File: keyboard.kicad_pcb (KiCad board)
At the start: 2 copper layers, 305.7 x 121 mm, 175 parts, among them J1 Conn_02x20_Odd_Even, J2 USB_C_Receptacle_16P

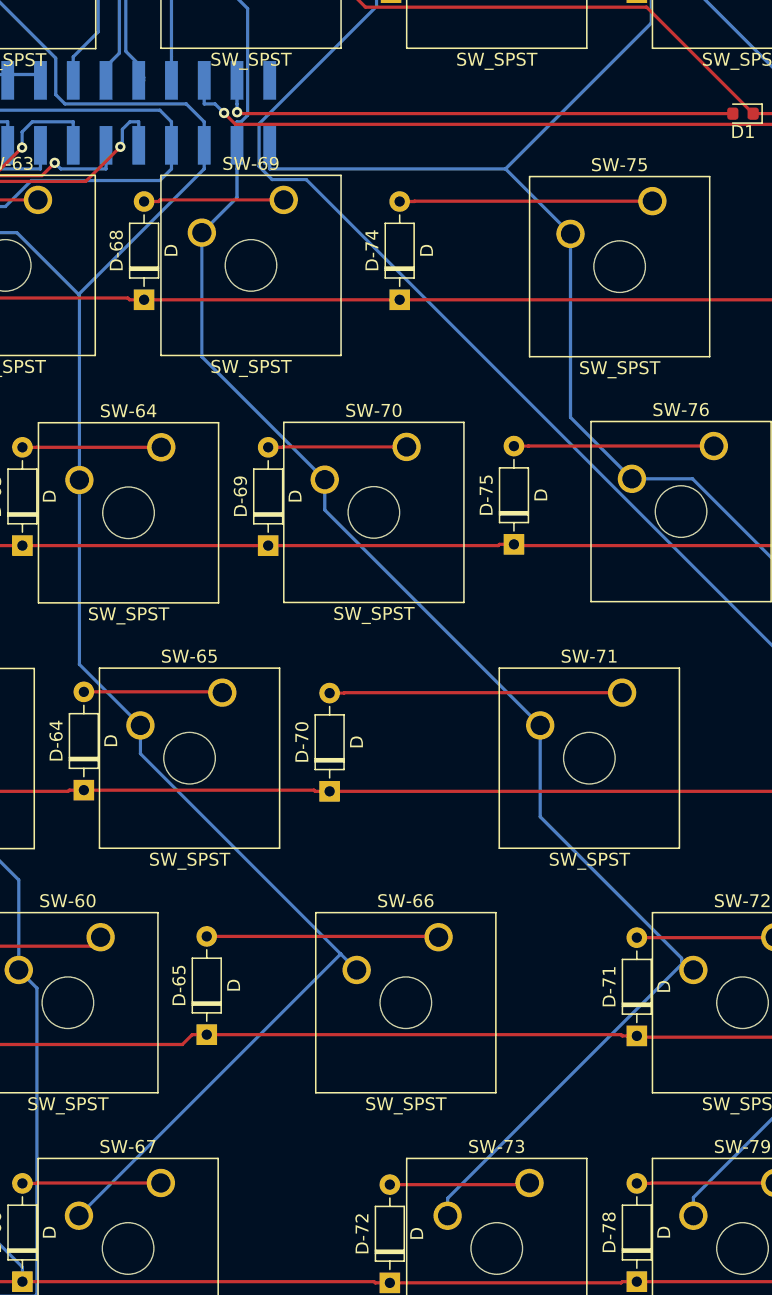
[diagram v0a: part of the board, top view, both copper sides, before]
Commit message: feat: update differential skew
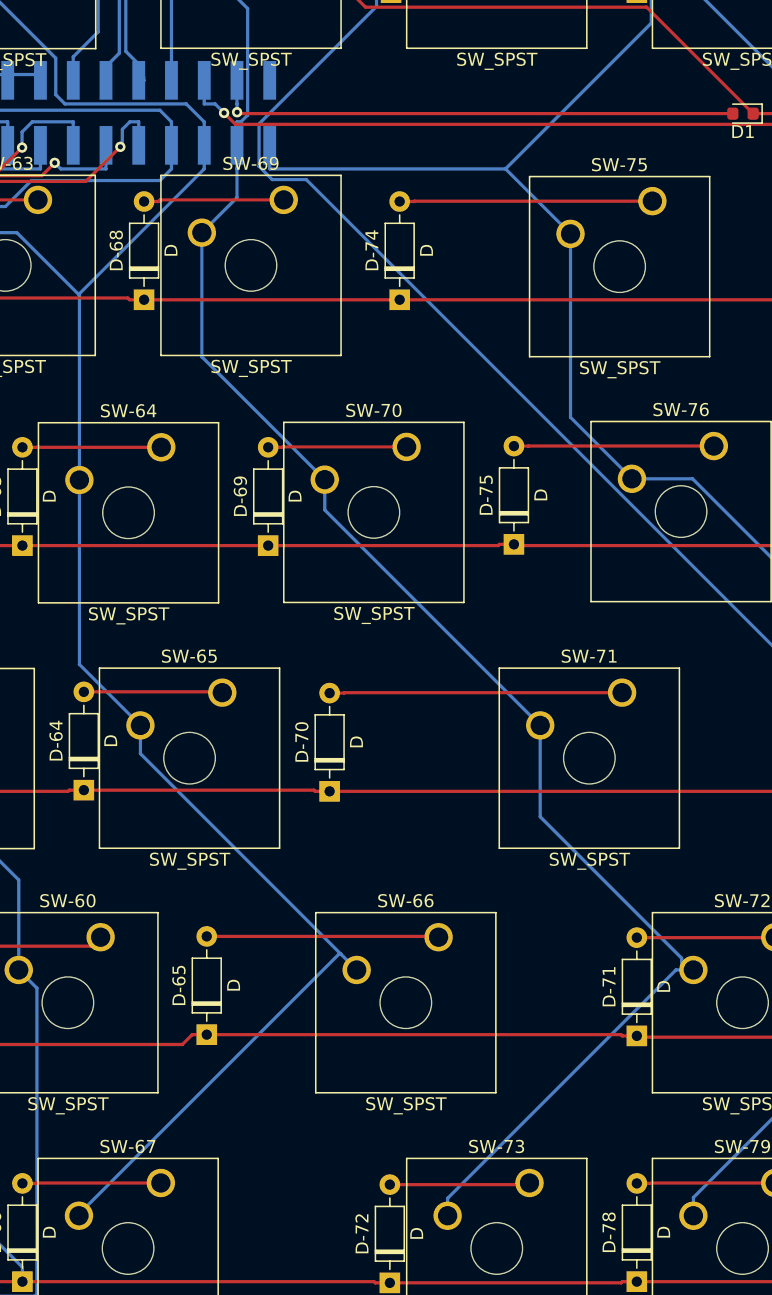
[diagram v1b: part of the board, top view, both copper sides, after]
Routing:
- net /COL13: track 127.2 -> 127.9 mm
